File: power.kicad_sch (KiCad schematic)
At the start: 42 parts

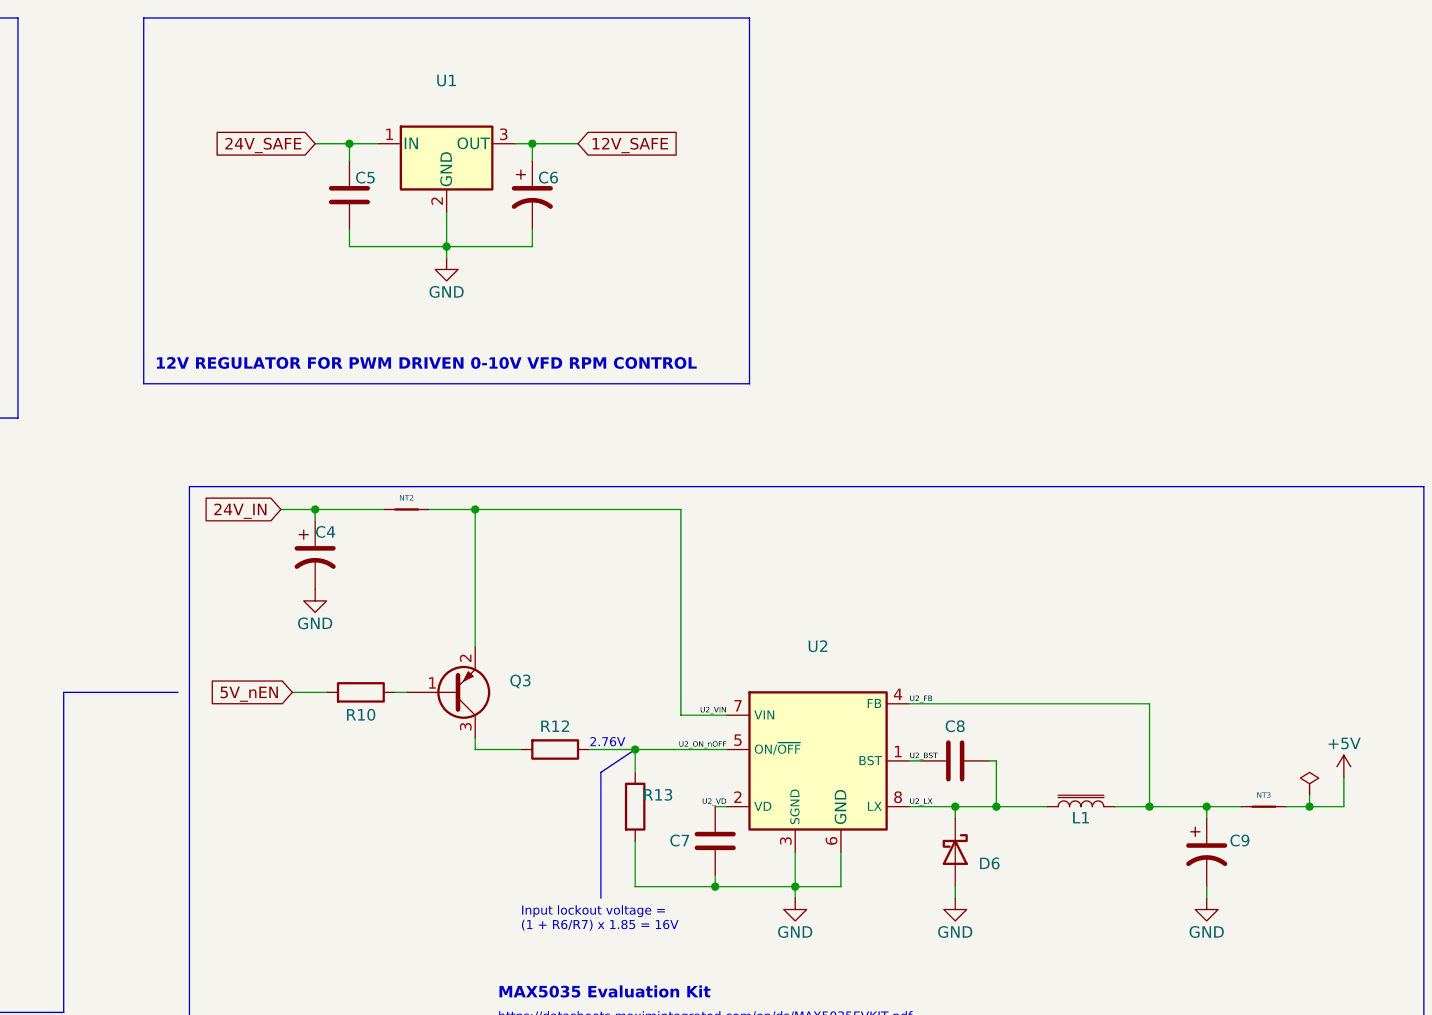
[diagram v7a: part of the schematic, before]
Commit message: Added 100n extra decoupling cap to PWM 12V reg.
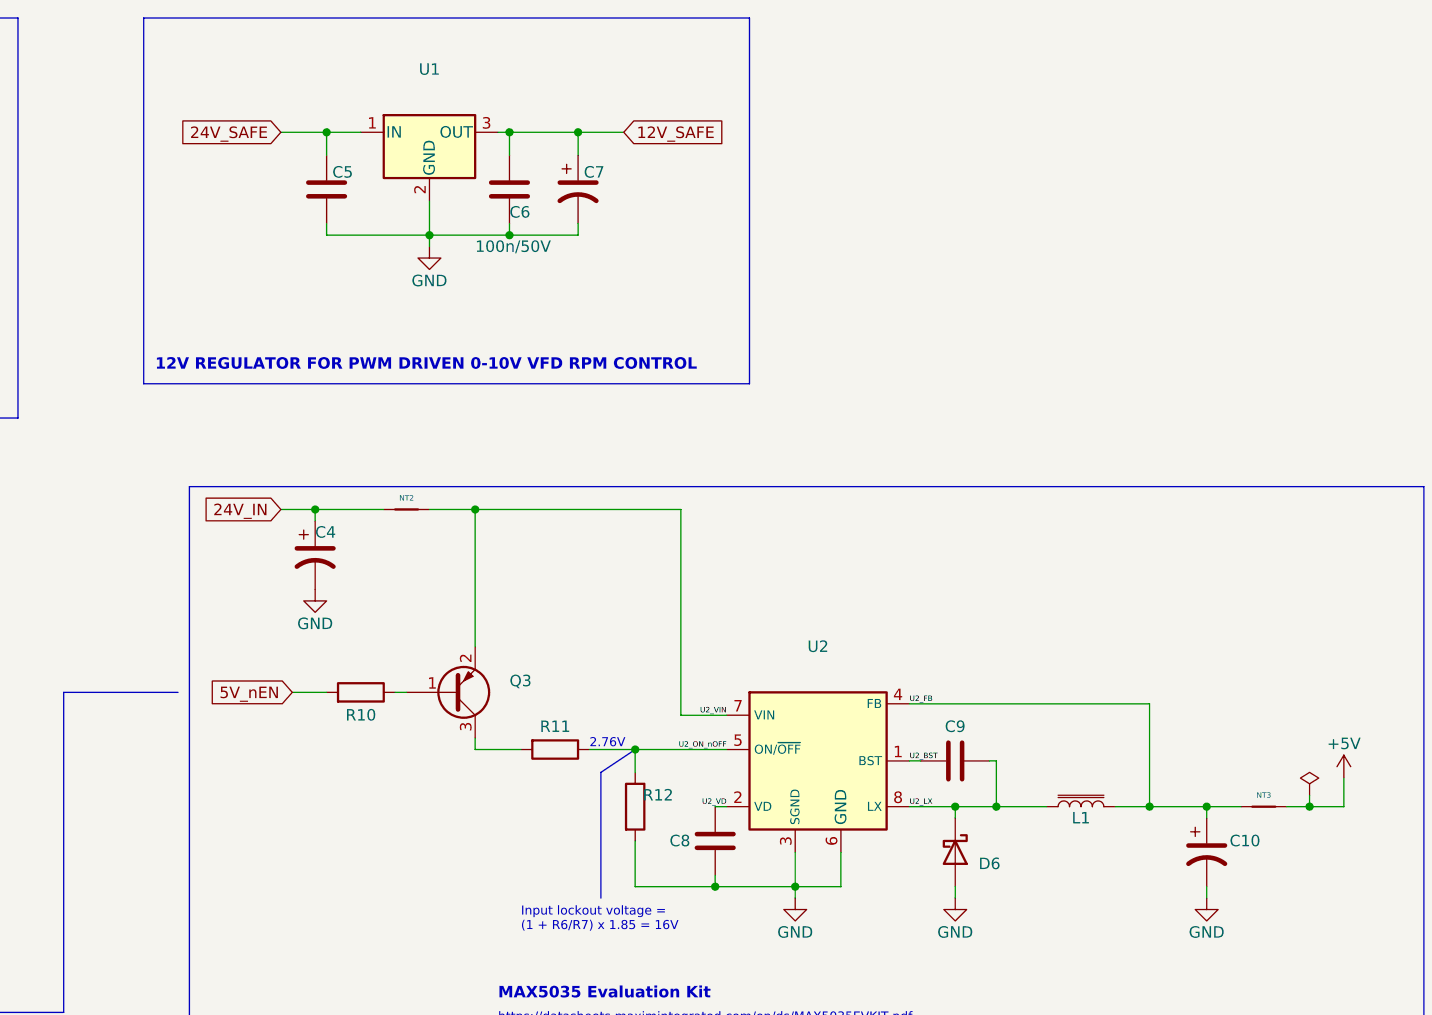
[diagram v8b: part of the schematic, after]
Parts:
- added C6: 100n/50V, Capacitor_SMD:C_0603_1608Metric, symbol Device:C
- C8: renamed from C7; E14PART 432210 -> (none)
- C9: renamed from C8; E14PART 432210 -> (none)
- renumbered C9 to C10, C6 to C7, R12 to R11, R13 to R12
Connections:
- net 12V_SAFE: now also C6.1
- net GND: now also C6.2
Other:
- moved on the sheet: C5, C7, U1
